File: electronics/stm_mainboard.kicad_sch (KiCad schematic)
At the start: 0 parts

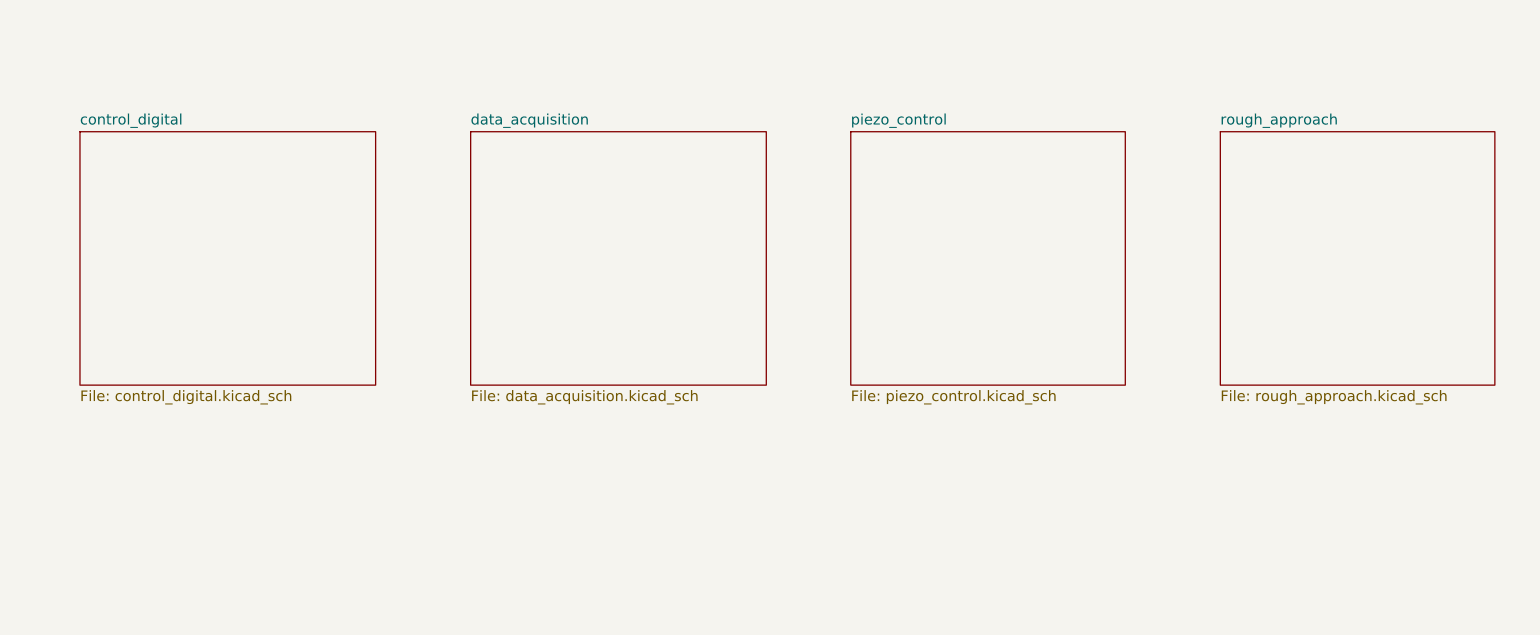
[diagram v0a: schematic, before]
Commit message: version en dos placas, pero con errores de tierra general. Se procede a versionar la PCB
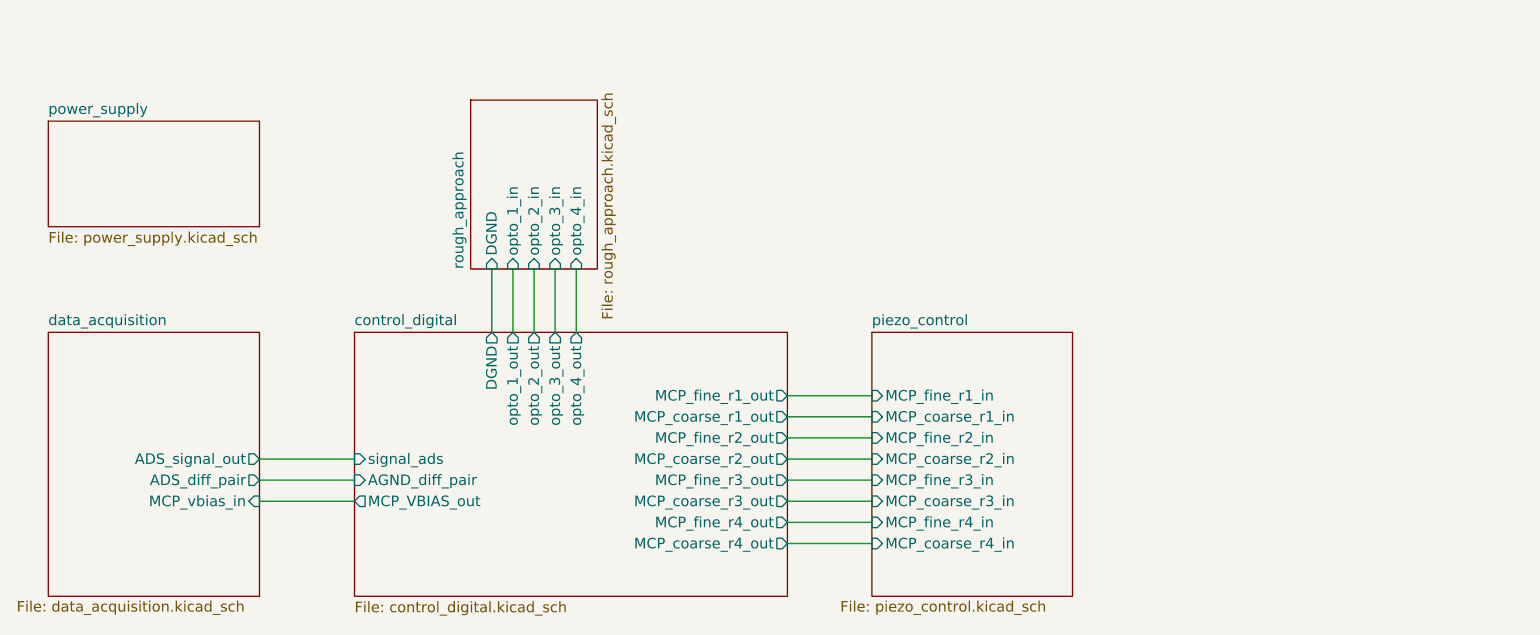
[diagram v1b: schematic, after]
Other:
- added sheet power_supply (power_supply.kicad_sch)
- sheet control_digital ports: added AGND_diff_pair, DGND, MCP_VBIAS_out, MCP_coarse_r1_out, MCP_coarse_r2_out, MCP_coarse_r3_out, MCP_coarse_r4_out, MCP_fine_r1_out, MCP_fine_r2_out, MCP_fine_r3_out, MCP_fine_r4_out, opto_1_out, opto_2_out, opto_3_out, opto_4_out, signal_ads; removed none
- sheet data_acquisition ports: added ADS_diff_pair, ADS_signal_out, MCP_vbias_in; removed none
- sheet piezo_control ports: added MCP_coarse_r1_in, MCP_coarse_r2_in, MCP_coarse_r3_in, MCP_coarse_r4_in, MCP_fine_r1_in, MCP_fine_r2_in, MCP_fine_r3_in, MCP_fine_r4_in; removed none
- sheet rough_approach ports: added DGND, opto_1_in, opto_2_in, opto_3_in, opto_4_in; removed none
